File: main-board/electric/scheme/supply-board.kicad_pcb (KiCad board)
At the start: 2 copper layers, 74 x 56 mm, 136 parts, among them K1 CONN_3, P1 PWR-IN, P10 TST, P11 TST, P12 PWR-IN, P13 CONN_4, P14 PWR-IN, P16 TST, P2 PWR-IN, P3 CONN_4, P4 cross board conn, P5 PWR-IN, P6 TST, P7 TST, P8 TST, P9 CONN_3X2, Q1 BC847, Q10 MOS_N, Q11 MOS_P, Q12 MOS_P, Q2 BC847, Q3 BC847, Q4 MOS_P, Q5 BC847, Q6 BC857, Q7 BC847, Q8 BC857, Q9 BC847, U1 NCP3063, U2 L293, U3 MINI-USB-B, X1 8MHz

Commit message: Routing...
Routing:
- net /buck+: track 20.0 -> 73.2 mm, vias 0 -> 2
- net /temperature: track 5.19 -> 13.5 mm
- net /boost-pwm: track 23.7 -> 25.7 mm
- net /buck-current: track 24.8 -> 26.7 mm
- net /solar: track 74.1 -> 75.2 mm

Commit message: Routing...
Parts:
- moved R46 1.37 mm to (161.7, 145.2), turned to 0 degrees
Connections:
- P9 pad 4: /buck-out-5v -> (no net)
- stm1 pad 13: /solar-volt -> /batt-volt
- stm1 pad 14: /batt-volt -> /buck-volt
- stm1 pad 15: /buck-volt -> /solar-volt
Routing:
- net /buck-out-5v: track 75.5 -> 142.5 mm, vias 0 -> 1
- net VDD: track 98.4 -> 155.8 mm, vias 1 -> 5
- net /batt-volt: track 1.91 -> 58.6 mm, vias 0 -> 1
- net /solar-volt: track 1.65 -> 51.2 mm, vias 0 -> 5
- net /buck-volt: track 1.65 -> 44.4 mm, vias 0 -> 1
- net GND: track 471.2 -> 483.0 mm
- net /boost-current: track 26.3 -> 30.6 mm
- net /buck-current: track 26.7 -> 30.3 mm
- net /solar: track 75.2 -> 78.4 mm
- net /temperature: track 13.5 -> 16.1 mm
- net /solar+: track 34.0 -> 35.9 mm
- net /buck+: track 73.2 -> 74.2 mm
- net /buck-pwm: track 32.8 -> 31.9 mm

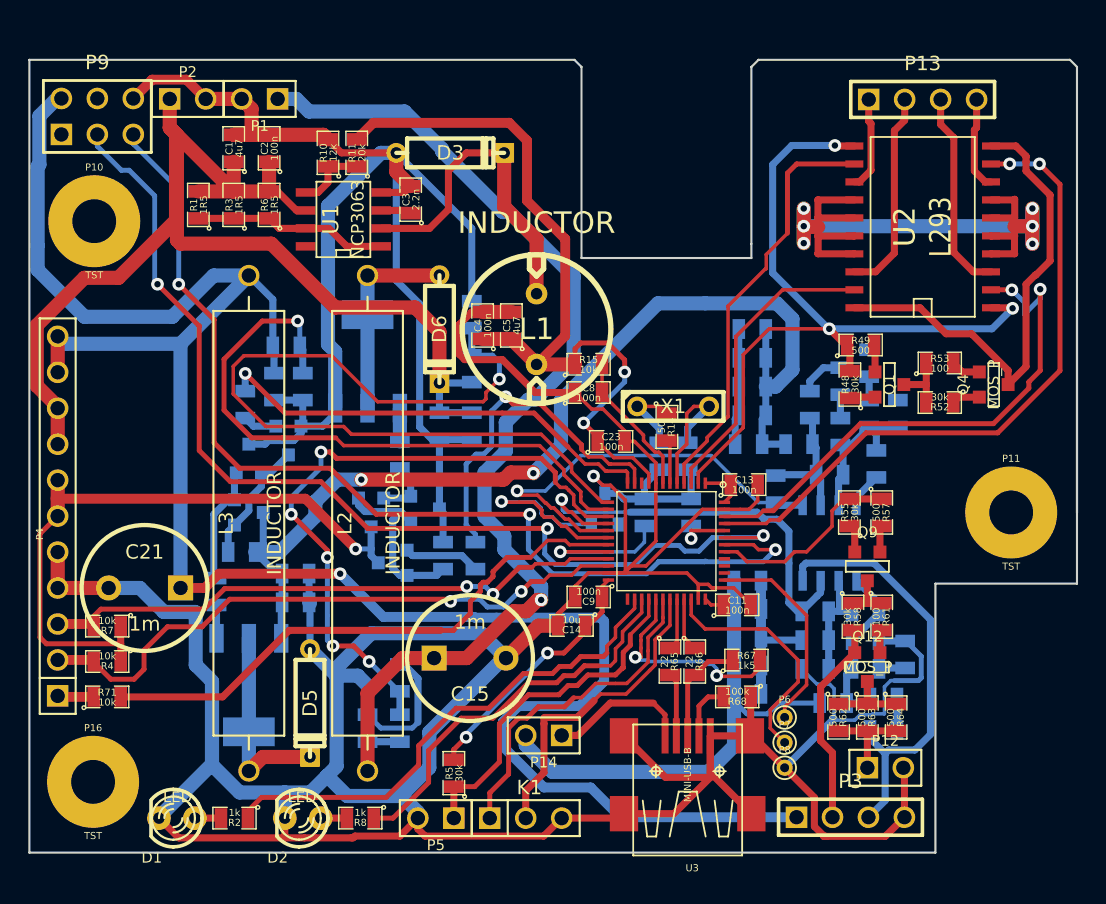
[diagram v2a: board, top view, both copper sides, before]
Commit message: Routing is done. Added GND zones. I'm going to add text right in copper layer.
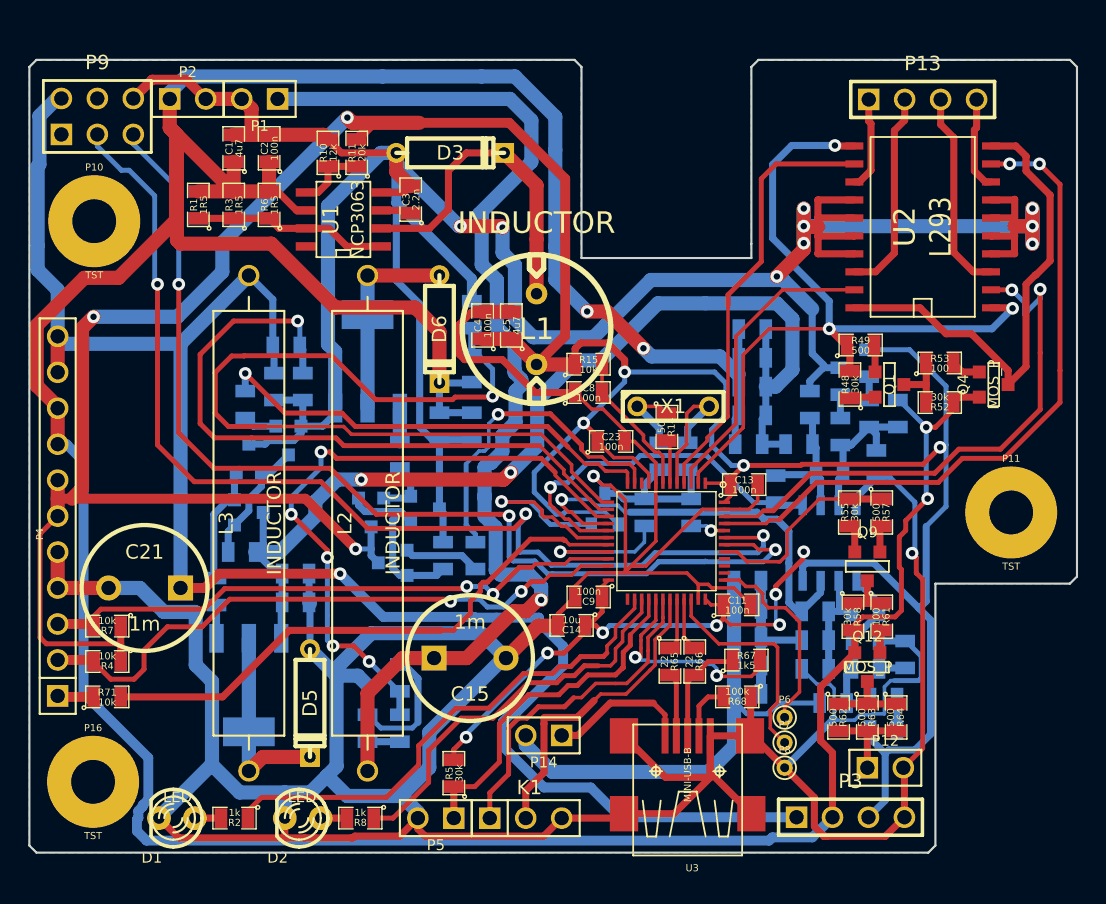
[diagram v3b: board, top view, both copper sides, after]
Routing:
- net +6V: track 126.7 -> 287.8 mm, vias 0 -> 4
- net VDD: track 155.8 -> 297.5 mm, vias 5 -> 14
- net GND: track 483.0 -> 558.1 mm, vias 7 -> 11
- net /buck-out-5v: track 142.5 -> 123.4 mm
- net /solar: track 78.4 -> 84.1 mm
- net /buck-current: track 30.3 -> 26.3 mm
- net /buck-volt: track 44.4 -> 48.1 mm
- net /sda-rpi: track 74.2 -> 77.8 mm
- net /boost-pwm: track 25.9 -> 22.9 mm
- net /batt-volt: track 58.6 -> 60.7 mm
- net /swd-io: track 17.1 -> 15.6 mm
- net /moto1: track 38.3 -> 39.7 mm
- net N-0000019: track 3.82 -> 2.49 mm
- net /moto2: track 46.8 -> 48.1 mm
- net /scl-rpi: track 77.0 -> 78.2 mm
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- added copper zone on B.Cu, net GND
- added copper zone on F.Cu, net GND
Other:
- outline, holes or cut-outs redrawn

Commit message: Added socket labels.
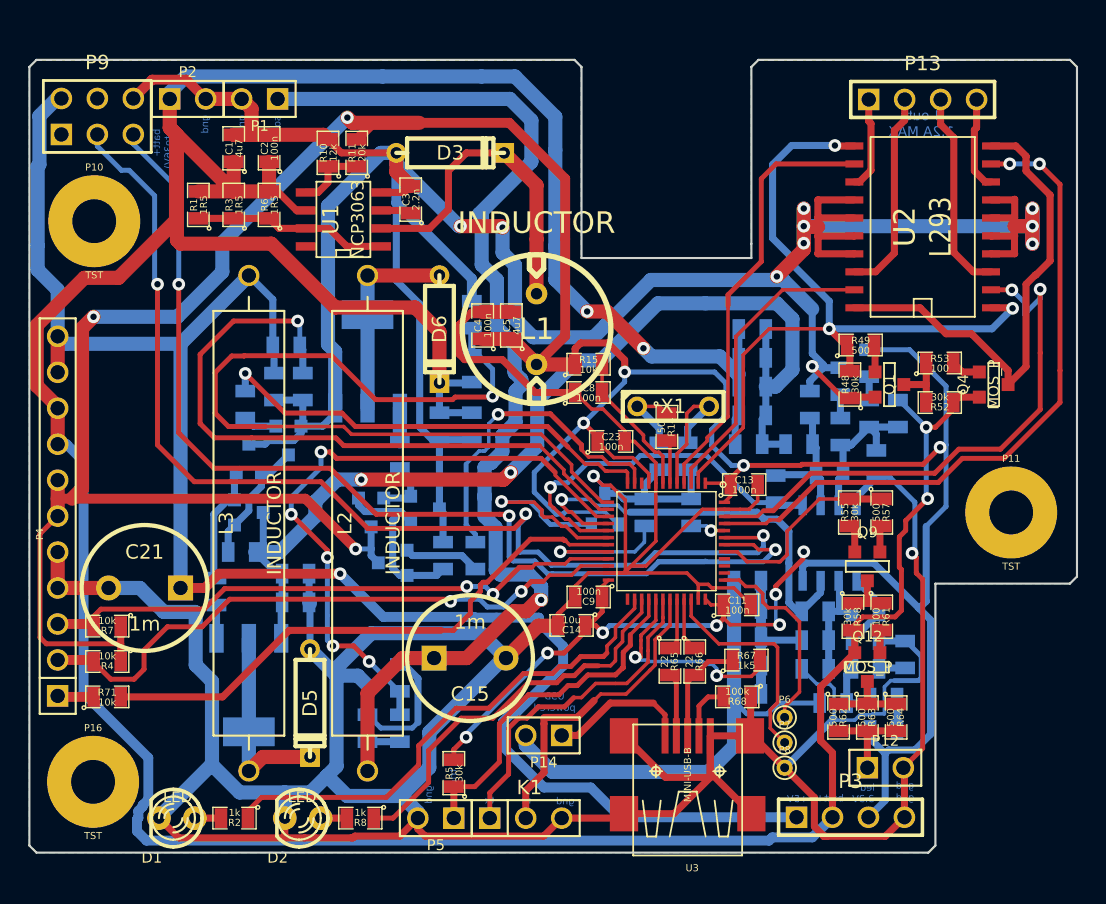
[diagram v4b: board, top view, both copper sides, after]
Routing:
- net GND: track 558.1 -> 562.5 mm, vias 11 -> 12
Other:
- board text added: "+5V"
- board text added: "3.3V"
- board text added: "4 outs 1.2A MAX"
- board text added: "USB powered"
- board text added: "batt+"
- board text added: "batt+ (5V to36V)"
- board text added: "gnd"
- board text added: "led"
- board text added: "rx"
- board text added: "solar"
- board text added: "trigger"
- board text added: "tx"
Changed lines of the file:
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@@
   (general
     (links 286)
-    (no_connects 1)
+    (no_connects 0)
     (area 127.606667 112.000001 242.964763 190.8)
     (thickness 1.6)
-    (drawings 51)
-    (tracks 1419)
+    (drawings 68)
+    (tracks 1425)
     (zones 0)
     (modules 136)
@@
     )
   )
+  (gr_text "USB\npowered" (at 180.6 170.35) (layer B.Cu)
+    (effects (font (size 0.5 0.5) (thickness 0.125)) (justify mirror))
+  )
+  (gr_text led (at 202.7 176.4) (layer B.Cu)
+    (effects (font (size 0.5 0.5) (thickness 0.125)) (justify mirror))
+  )
+  (gr_text gnd (at 205.35 176.25) (layer B.Cu)
+    (effects (font (size 0.5 0.5) (thickness 0.125)) (justify mirror))
+  )
+  (gr_text gnd (at 205.35 177.1) (layer B.Cu)
+    (effects (font (size 0.5 0.5) (thickness 0.125)) (justify mirror))
+  )
+  (gr_text 3.3V (at 202.4 177.2) (layer B.Cu)
+    (effects (font (size 0.5 0.5) (thickness 0.125)) (justify mirror))
+  )
+  (gr_text batt+ (at 200.05 177.15) (layer B.Cu)
+    (effects (font (size 0.5 0.5) (thickness 0.125)) (justify mirror))
+  )
+  (gr_text +5V (at 197.75 177.2) (layer B.Cu)
+    (effects (font (size 0.5 0.5) (thickness 0.125)) (justify mirror))
+  )
+  (gr_text gnd (at 181.35 177.35) (layer B.Cu)
+    (effects (font (size 0.5 0.5) (thickness 0.125)) (justify mirror))
+  )
+  (gr_text rx (at 178.6 177.3) (layer B.Cu)
+    (effects (font (size 0.5 0.5) (thickness 0.125)) (justify mirror))
+  )
+  (gr_text tx (at 176 177.3) (layer B.Cu)
+    (effects (font (size 0.5 0.5) (thickness 0.125)) (justify mirror))
+  )
+  (gr_text trigger (at 173.45 176.25 90) (layer B.Cu)
+    (effects (font (size 0.5 0.5) (thickness 0.125)) (justify mirror))
+  )
+  (gr_text gnd (at 171.7 176.9 90) (layer B.Cu)
+    (effects (font (size 0.5 0.5) (thickness 0.125)) (justify mirror))
+  )
+  (gr_text solar (at 161 129.8 90) (layer B.Cu)
+    (effects (font (size 0.5 0.5) (thickness 0.125)) (justify mirror))
+  )
+  (gr_text gnd (at 158.5 129.55 90) (layer B.Cu)
+    (effects (font (size 0.5 0.5) (thickness 0.125)) (justify mirror))
+  )
+  (gr_text gnd (at 155.9 129.55 90) (layer B.Cu)
+    (effects (font (size 0.5 0.5) (thickness 0.125)) (justify mirror))
+  )
+  (gr_text "batt+ \n(5V to36V)" (at 152.9 130.85 90) (layer B.Cu)
+    (effects (font (size 0.5 0.5) (thickness 0.125)) (justify mirror))
+  )
+  (gr_text "4 outs\n1.2A MAX\n" (at 206.5 129.5) (layer B.Cu)
+    (effects (font (size 0.7 0.7) (thickness 0.175)) (justify mirror))
+  )
   (gr_line (start 144 181) (end 207 181) (angle 90) (layer Edge.Cuts) (width 0.15))
   (gr_line (start 143.5 125.5) (end 143.5 180.5) (angle 90) (layer Edge.Cuts) (width 0.15))
@@
   (segment (start 184.40298 159.24892) (end 181.64892 159.24892) (width 0.25) (layer F.Cu) (net 43))
   (segment (start 181.64892 159.24892) (end 181.35 158.95) (width 0.25) (layer F.Cu) (net 43))
+  (segment (start 201.458 148.8905) (end 200.9905 148.8905) (width 0.35) (layer F.Cu) (net 44))
+  (segment (start 198.8 146.65) (end 199.6 146.65) (width 0.35) (layer B.Cu) (net 44))
+  (via (at 198.8 146.65) (size 0.9) (layers F.Cu B.Cu) (net 44))
+  (segment (start 198.8 146.7) (end 198.8 146.65) (width 0.35) (layer F.Cu) (net 44))
+  (segment (start 200.9905 148.8905) (end 198.8 146.7) (width 0.35) (layer F.Cu) (net 44))
   (segment (start 184.2 143.75) (end 183.35 144.6) (width 1) (layer B.Cu) (net 44))
   (segment (start 176.825 136.75) (end 173.95 136.75) (width 1) (layer F.Cu) (net 44))
@@
   (segment (start 174.752 140.452) (end 169.418 135.118) (width 0.7) (layer B.Cu) (net 44))
   (segment (start 169.418 135.118) (end 169.418 131.572) (width 0.7) (layer B.Cu) (net 44))
-  (segment (start 199.6 146.7485) (end 199.6 146.55) (width 0.5) (layer B.Cu) (net 44))
-  (segment (start 198.8 142.6) (end 196.75 140.55) (width 0.5) (layer B.Cu) (net 44))
-  (segment (start 198.8 145.75) (end 198.8 142.6) (width 0.5) (layer B.Cu) (net 44))
+  (segment (start 199.6 146.7485) (end 199.6 146.65) (width 0.5) (layer B.Cu) (net 44))
+  (segment (start 199.6 146.65) (end 199.6 146.55) (width 0.5) (layer B.Cu) (net 44))
   (segment (start 199.6 146.55) (end 198.8 145.75) (width 0.5) (layer B.Cu) (net 44))
+  (segment (start 198.8 145.75) (end 198.8 142.6) (width 0.5) (layer B.Cu) (net 44))
+  (segment (start 198.8 142.6) (end 196.75 140.55) (width 0.5) (layer B.Cu) (net 44))
   (segment (start 155.956 127.762) (end 154.594 126.4) (width 0.7) (layer F.Cu) (net 44))
   (segment (start 152.17 126.4) (end 150.84 127.73) (width 0.7) (layer F.Cu) (net 44))

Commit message: Added acelerometer (it's optional).
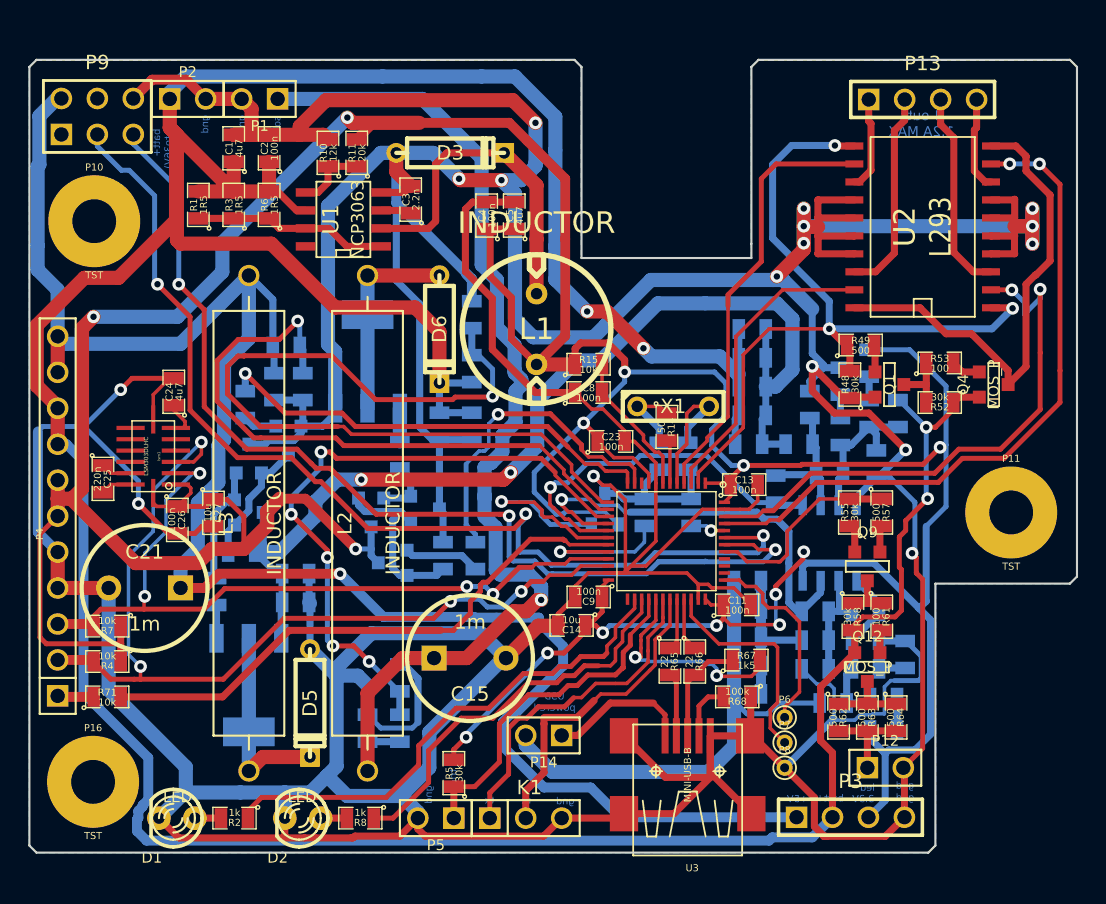
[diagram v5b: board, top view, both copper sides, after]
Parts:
- added C24: 4u7, SM0805, F.Cu at (153.7, 148.4)
- added C25: 220n, SM0805, F.Cu at (148.7, 154.6)
- added C26: 100n, SM0805, F.Cu at (153.9, 157.5)
- added C27: 10u, SM0805, F.Cu at (156.5, 157.0)
- added lsm1: LSM303DLHC, lga14-0.3mm, F.Cu at (152.2, 153.0)
- moved C4 7.77 mm to (175.8, 136.0)
- moved C5 7.77 mm to (177.8, 136.0)
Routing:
- net GND: track 562.5 -> 637.1 mm, vias 12 -> 16
- net VDD: track 297.5 -> 324.1 mm
- net /sda-int: track 44.2 -> 65.4 mm, vias 2 -> 4
- net /scl-int: track 42.5 -> 55.8 mm, vias 2 -> 4
- net /buck-out-5v: track 123.4 -> 130.2 mm
- net /solar: track 84.1 -> 77.4 mm
- net /buck-volt: track 48.1 -> 44.5 mm
- net /sda-rpi: track 77.8 -> 75.0 mm
- net N-0000054: track 0.00 -> 2.49 mm
- net /batt-volt: track 60.7 -> 58.4 mm
- net N-0000052: track 0.00 -> 2.18 mm
- net N-0000053: track 0.00 -> 2.18 mm
- net /scl-rpi: track 78.2 -> 76.0 mm
- net N-0000027: track 23.4 -> 24.2 mm

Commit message: Moved peripherial sockets closer to outer board edge.
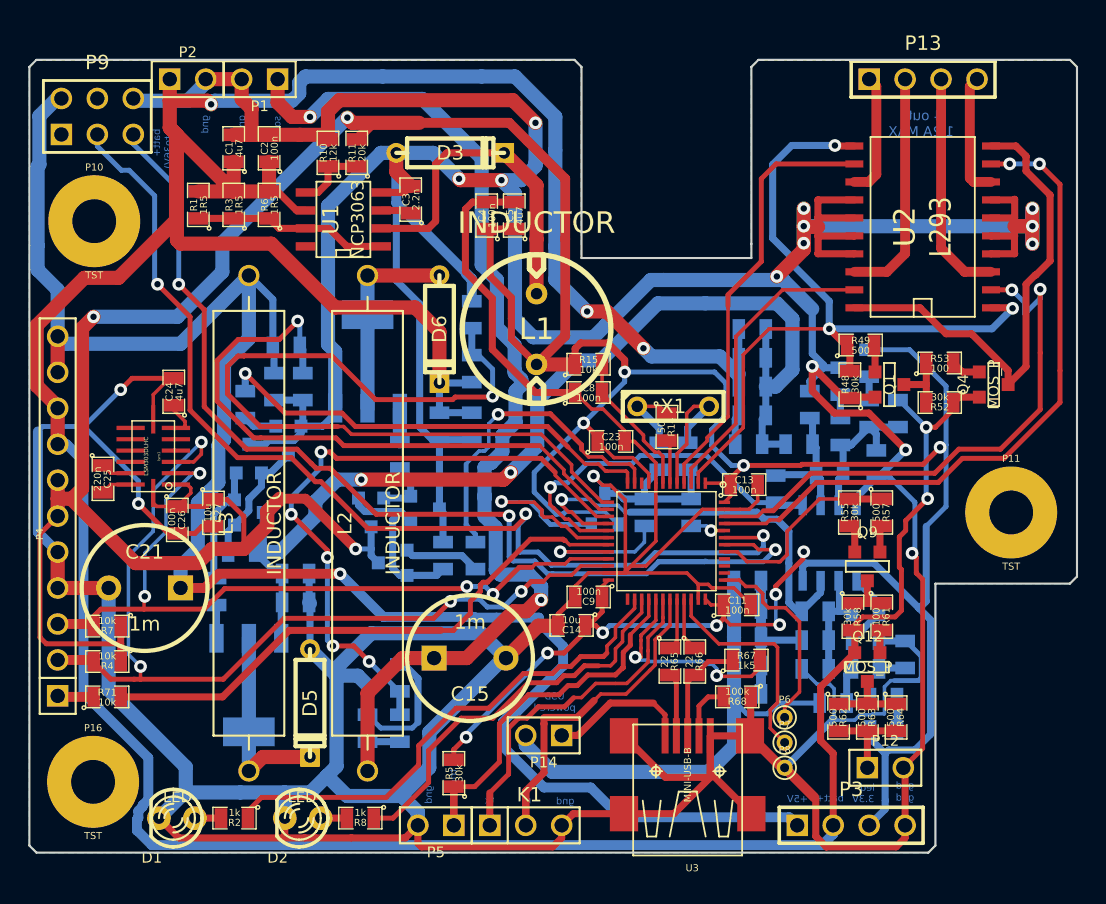
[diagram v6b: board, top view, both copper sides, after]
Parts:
- moved P13 1.44 mm to (206.6, 126.4)
- moved P1 1.40 mm to (159.8, 126.4)
- moved P2 1.40 mm to (154.7, 126.4)
- moved P3 0.57 mm to (201.5, 179.1)
- moved K1 0.51 mm to (178.6, 179.1)
- moved P5 0.51 mm to (172.2, 179.1)
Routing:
- net GND: track 637.1 -> 641.6 mm
- net /just-power-source: track 24.8 -> 27.6 mm
- net /solar: track 77.4 -> 80.0 mm, vias 1 -> 2
- net /rx: track 27.4 -> 29.8 mm
- net /tx: track 23.6 -> 25.9 mm
- net /out2: track 6.61 -> 8.80 mm
- net /out4: track 6.58 -> 8.71 mm
- net /out3: track 14.5 -> 16.4 mm
- net /out1: track 14.4 -> 16.2 mm
- net +6V: track 287.8 -> 288.7 mm, vias 4 -> 5
- net VDD: track 324.1 -> 324.7 mm

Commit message: Raplaced power mosfets with sot23 transistors because of their max current and very low resistance.
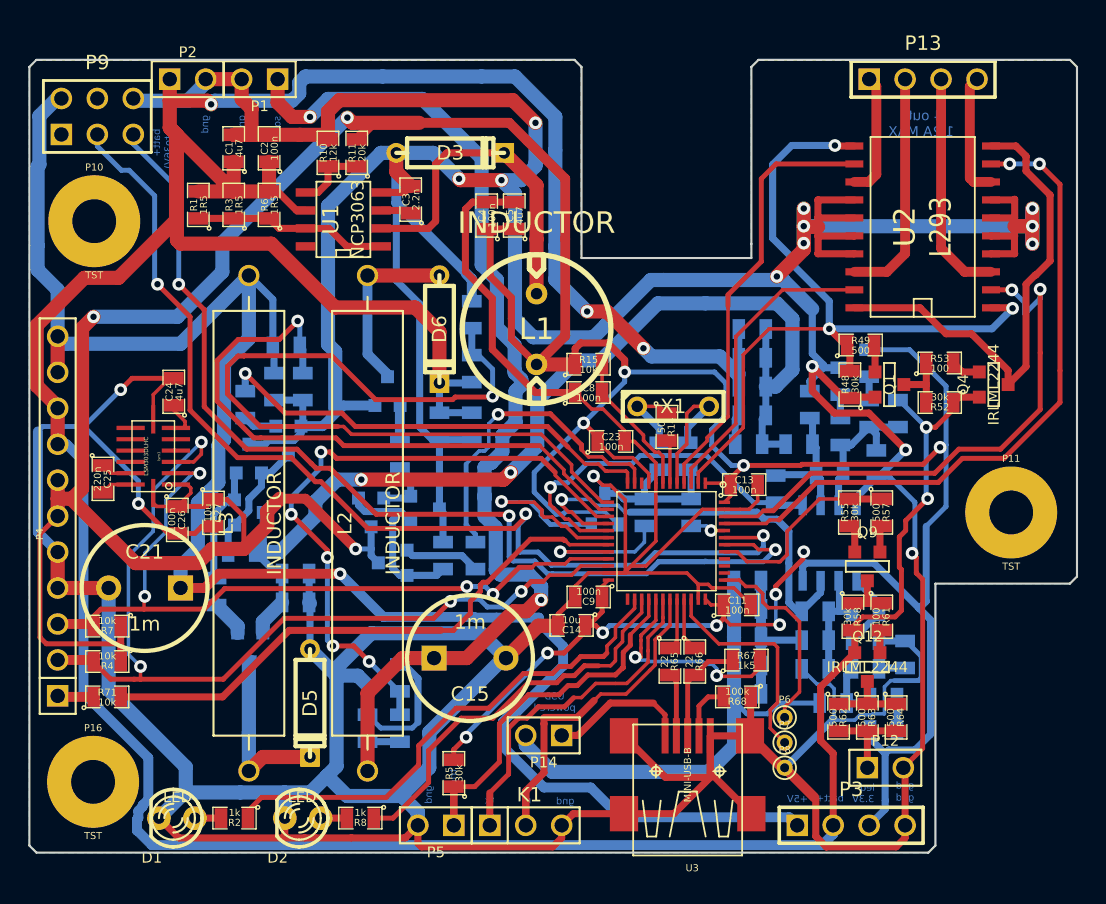
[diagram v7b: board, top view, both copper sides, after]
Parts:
- Q10: value MOS_N -> IRLML2502; footprint SOT223-GDSD -> SOT23GDS
- Q11: value MOS_P -> IRLML2244; footprint SOT223-GDSD -> SOT23GDS
- Q12, Q4: value MOS_P -> IRLML2244
- moved Q11 2.67 mm to (159.1, 166.5), turned to 180 degrees
- moved Q10 2.53 mm to (168.8, 148.4), turned to 0 degrees
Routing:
- net GND: track 641.6 -> 647.4 mm
- net N-000004: track 14.5 -> 12.8 mm
- net N-000008: track 14.1 -> 12.7 mm
